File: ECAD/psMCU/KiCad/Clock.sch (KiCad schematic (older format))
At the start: 0 parts

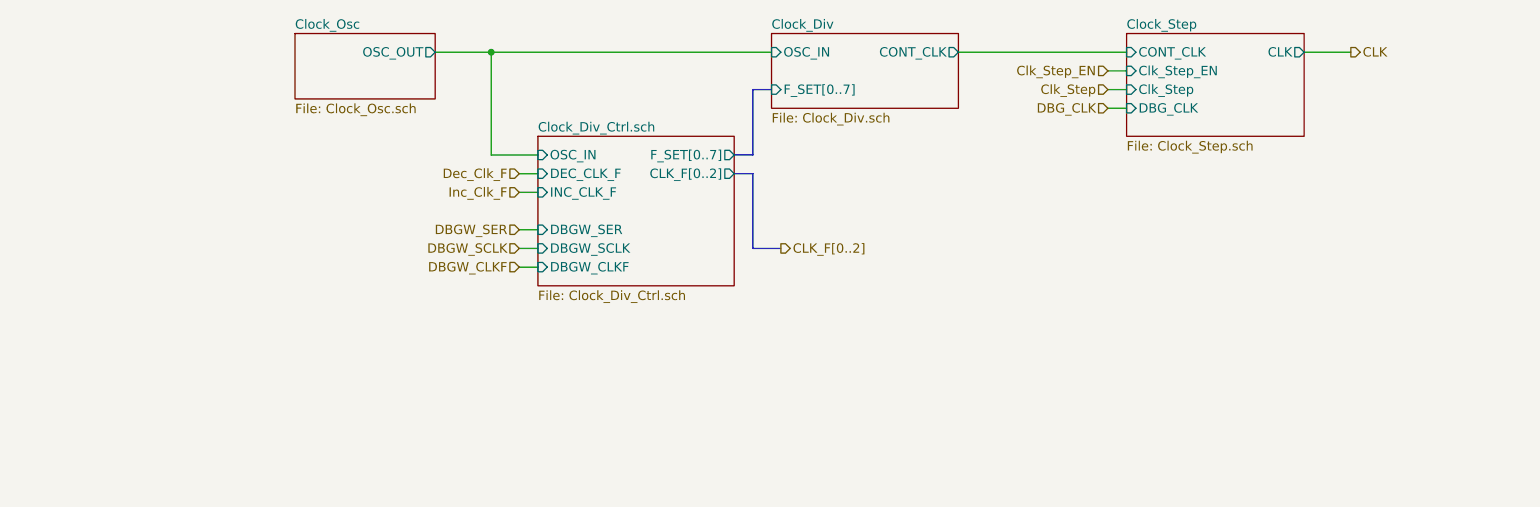
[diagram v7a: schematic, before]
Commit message: Sch: More cleanup, fixed page descriptions.
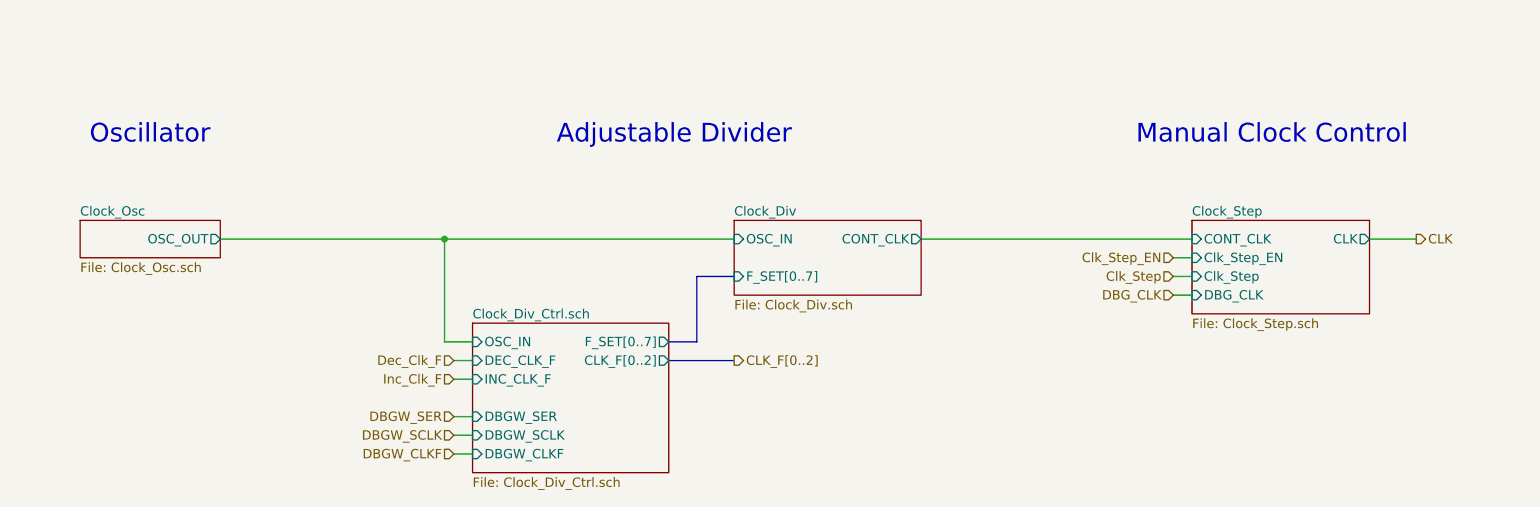
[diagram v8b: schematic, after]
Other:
- note added: "Adjustable Divider"
- note added: "Manual Clock Control"
- note added: "Oscillator"
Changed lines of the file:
@@
 Sheet 97 109
 Title "psMCU"
-Date "2022-02-13"
+Date "2022-02-20"
 Rev "v1.1"
 Comp "Philipp Schilk"
@@
 Comment4 "Variable frequency clock generation."
 $EndDescr
-Text HLabel 6000 3200 2    50   Output ~ 0
+Text HLabel 5750 3800 2    50   Output ~ 0
 CLK_F[0..2]
 Wire Bus Line
-	5850 2800 5850 3200
-Wire Bus Line
-	5850 2700 5850 2350
+	5550 3700 5550 3350
 Wire Wire Line
-	4450 2700 4450 2150
-Wire Wire Line
-	6950 2150 7850 2150
+	4200 3700 4200 3150
 $Sheet
-S 5950 2050 1000 400
+S 5750 3050 1000 400
 U 5FFB4D29
 F0 "Clock_Div" 50
 F1 "Clock_Div.sch" 50
-F2 "OSC_IN" I L 5950 2150 50
-F3 "CONT_CLK" O R 6950 2150 50
-F4 "F_SET[0..7]" I L 5950 2350 50
+F2 "OSC_IN" I L 5750 3150 50
+F3 "CONT_CLK" O R 6750 3150 50
+F4 "F_SET[0..7]" I L 5750 3350 50
 $EndSheet
 Wire Wire Line
-	4450 2700 4700 2700
+	4200 3700 4350 3700
 $Sheet
-S 4700 2600 1050 800
+S 4350 3600 1050 800
 U 60010AFF
 F0 "Clock_Div_Ctrl.sch" 50
 F1 "Clock_Div_Ctrl.sch" 50
-F2 "INC_CLK_F" I L 4700 2900 50
-F3 "DEC_CLK_F" I L 4700 2800 50
-F4 "OSC_IN" I L 4700 2700 50
-F5 "F_SET[0..7]" O R 5750 2700 50
-F6 "CLK_F[0..2]" O R 5750 2800 50
-F7 "DBGW_SER" I L 4700 3100 50
-F8 "DBGW_SCLK" I L 4700 3200 50
-F9 "DBGW_CLKF" I L 4700 3300 50
+F2 "INC_CLK_F" I L 4350 3900 50
+F3 "DEC_CLK_F" I L 4350 3800 50
+F4 "OSC_IN" I L 4350 3700 50
+F5 "F_SET[0..7]" O R 5400 3700 50
+F6 "CLK_F[0..2]" O R 5400 3800 50
+F7 "DBGW_SER" I L 4350 4100 50
+F8 "DBGW_SCLK" I L 4350 4200 50
+F9 "DBGW_CLKF" I L 4350 4300 50
 $EndSheet
 Wire Wire Line
-	4700 2900 4600 2900
+	4350 3900 4250 3900
 Wire Wire Line
-	4600 2800 4700 2800
+	4250 3800 4350 3800
 Wire Wire Line
-	7750 2350 7850 2350
+	8100 3350 8200 3350
 Wire Wire Line
-	7750 2250 7850 2250
+	8100 3250 8200 3250
 Wire Wire Line
-	9050 2150 8800 2150
+	9400 3150 9150 3150
 $Sheet
-S 3400 2050 750  350
+S 2250 3050 750  200
 U 5FFC76CA
 F0 "Clock_Osc" 50
 F1 "Clock_Osc.sch" 50
-F2 "OSC_OUT" O R 4150 2150 50
+F2 "OSC_OUT" O R 3000 3150 50
 $EndSheet
 $Sheet
-S 7850 2050 950  550
+S 8200 3050 950  500
 U 5FFAAF6D
 F0 "Clock_Step" 50
 F1 "Clock_Step.sch" 50
-F2 "CLK" O R 8800 2150 50
-F3 "CONT_CLK" I L 7850 2150 50
-F4 "Clk_Step_EN" I L 7850 2250 50
-F5 "Clk_Step" I L 7850 2350 50
-F6 "DBG_CLK" I L 7850 2450 50
+F2 "CLK" O R 9150 3150 50
+F3 "CONT_CLK" I L 8200 3150 50
+F4 "Clk_Step_EN" I L 8200 3250 50
+F5 "Clk_Step" I L 8200 3350 50
+F6 "DBG_CLK" I L 8200 3450 50
 $EndSheet
-Text HLabel 4600 2800 0    50   Input ~ 0
+Text HLabel 4250 3800 0    50   Input ~ 0
 Dec_Clk_F
-Text HLabel 4600 2900 0    50   Input ~ 0
+Text HLabel 4250 3900 0    50   Input ~ 0
 Inc_Clk_F
-Text HLabel 7750 2350 0    50   Input ~ 0
+Text HLabel 8100 3350 0    50   Input ~ 0
 Clk_Step
-Text HLabel 7750 2250 0    50   Input ~ 0
+Text HLabel 8100 3250 0    50   Input ~ 0
 Clk_Step_EN
-Text HLabel 9050 2150 2    50   Output ~ 0
+Text HLabel 9400 3150 2    50   Output ~ 0
 CLK
-Wire Wire Line
-	4450 2150 5950 2150
-Wire Bus Line
-	5950 2350 5850 2350
-Wire Bus Line
-	5850 2700 5750 2700
-Wire Bus Line
-	5750 2800 5850 2800
-Wire Bus Line
-	5850 3200 6000 3200
-Wire Wire Line
-	4150 2150 4450 2150
-Connection ~ 4450 2150
-Text HLabel 7750 2450 0    50   Input ~ 0
+Text HLabel 8100 3450 0    50   Input ~ 0
 DBG_CLK
 Wire Wire Line
-	7850 2450 7750 2450
+	8200 3450 8100 3450
 Wire Wire Line
-	4700 3100 4600 3100
+	4350 4100 4250 4100
 Wire Wire Line
-	4700 3200 4600 3200
+	4350 4200 4250 4200
 Wire Wire Line
-	4700 3300 4600 3300
-Text HLabel 4600 3100 0    50   Input ~ 0
+	4350 4300 4250 4300
+Text HLabel 4250 4100 0    50   Input ~ 0
 DBGW_SER
-Text HLabel 4600 3200 0    50   Input ~ 0
+Text HLabel 4250 4200 0    50   Input ~ 0
 DBGW_SCLK
-Text HLabel 4600 3300 0    50   Input ~ 0
+Text HLabel 4250 4300 0    50   Input ~ 0
 DBGW_CLKF
+Wire Bus Line
+	5400 3700 5550 3700
+Wire Bus Line
+	5550 3350 5750 3350
+Wire Wire Line
+	4200 3150 5750 3150
+Wire Bus Line
+	5400 3800 5750 3800
+Wire Wire Line
+	3000 3150 4200 3150
+Connection ~ 4200 3150
+Wire Wire Line
+	6750 3150 8200 3150
+Text Notes 2300 2650 0    100  ~ 0
+Oscillator
+Text Notes 4800 2650 0    100  ~ 0
+Adjustable Divider
+Text Notes 7900 2650 0    100  ~ 0
+Manual Clock Control
 $EndSCHEMATC
